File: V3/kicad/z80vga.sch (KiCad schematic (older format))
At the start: 14 parts, among them J1000 Barrel_Jack_Switch, U1000 L7805, U1001 TL760M33

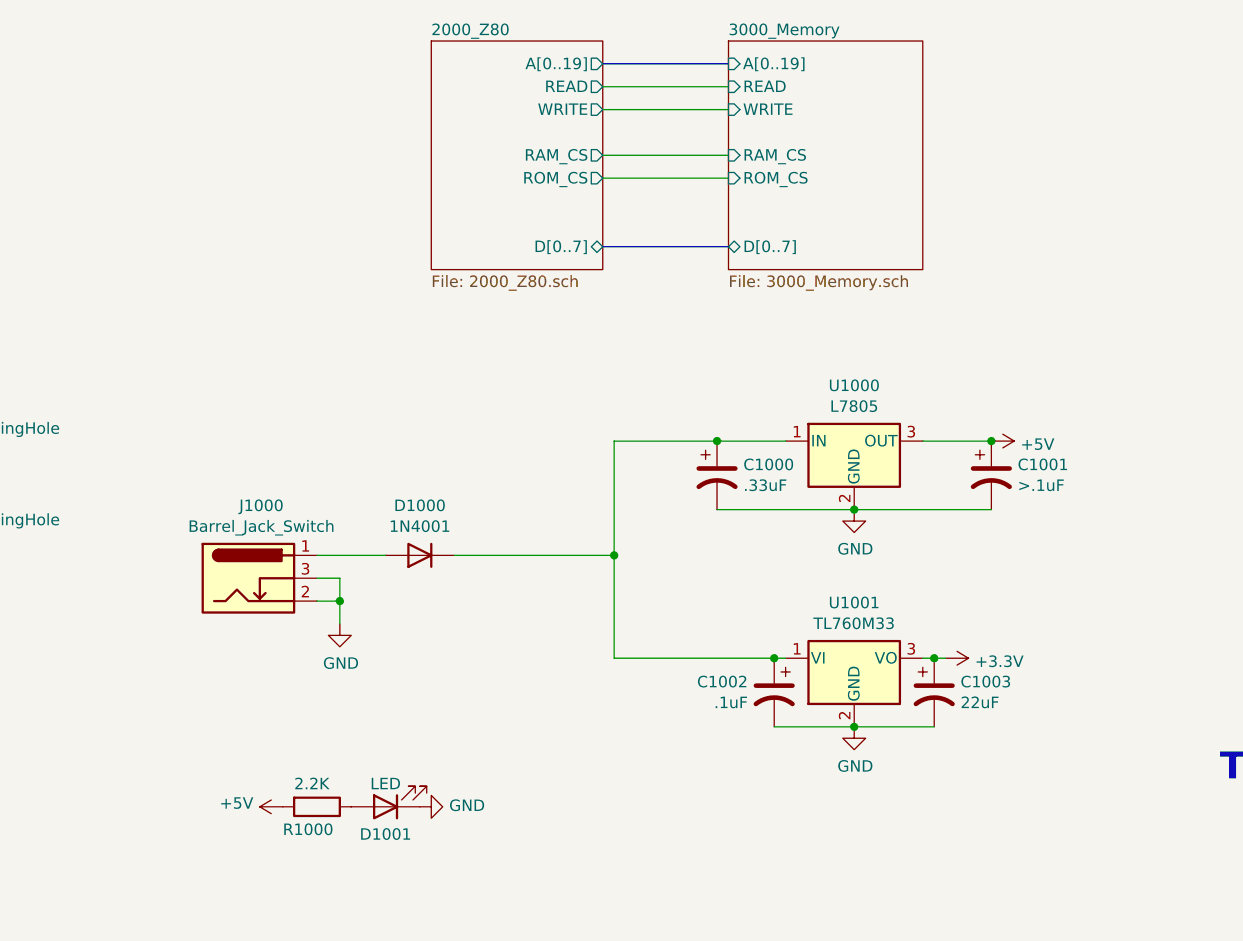
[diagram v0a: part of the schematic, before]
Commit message: 3 1 1 m memory (#15)
* moved EEPROM files to /old

* Reworking 3.0 board

* changed footprint on RAM chip

* cleared out old memory traces

* started on rerouting

* on to autoroute

* little more cleanup

* more cleanup

* ill let the autoroute do the rest

* reroute complete

* made PQFP leads fatter

* Updated GAL logic

* Design Rule Check

* Minor pcb touch up

* gerber files

* just totally redid the whole thing

* More rearranging

* added a few caps

* Routed ROM and RAM together

* more routing

* more routes

* A lot of disorganized changes

* 3.1 CSIO SPI Bus (#9)

* Updated SPI to use CPU signals

8 bit register chip controls CS lines

* Renamed and added caps to SD page

* Cleanup

* 3.1 Resistor Replacement (#10)

* First two R arrays

* Added one more r array

* added cap for SPI FF

* Extended cpu pads (#12)

* 3.1 fix sheet hierarchy (#13)

* Fixed Schematic Heirarchy issue

* some footprints re-added to board

* Add footprints added

* Minor changes

* 3.1 redraw cpu courtyard (#14)

* moved all crtyd lines to same place in file

* Duplicate lines were causing issues

* Added pin header for SPI lines

* routed last of non-bus lines

* attempted to route memory lines

* Added new symbol and footprint

* CTS0 no longer drives an LED

* Final cleanup before memory routing

* got CTS0 and RTS mixed up

* Removed extra led from board

* Updated signature

* small changes
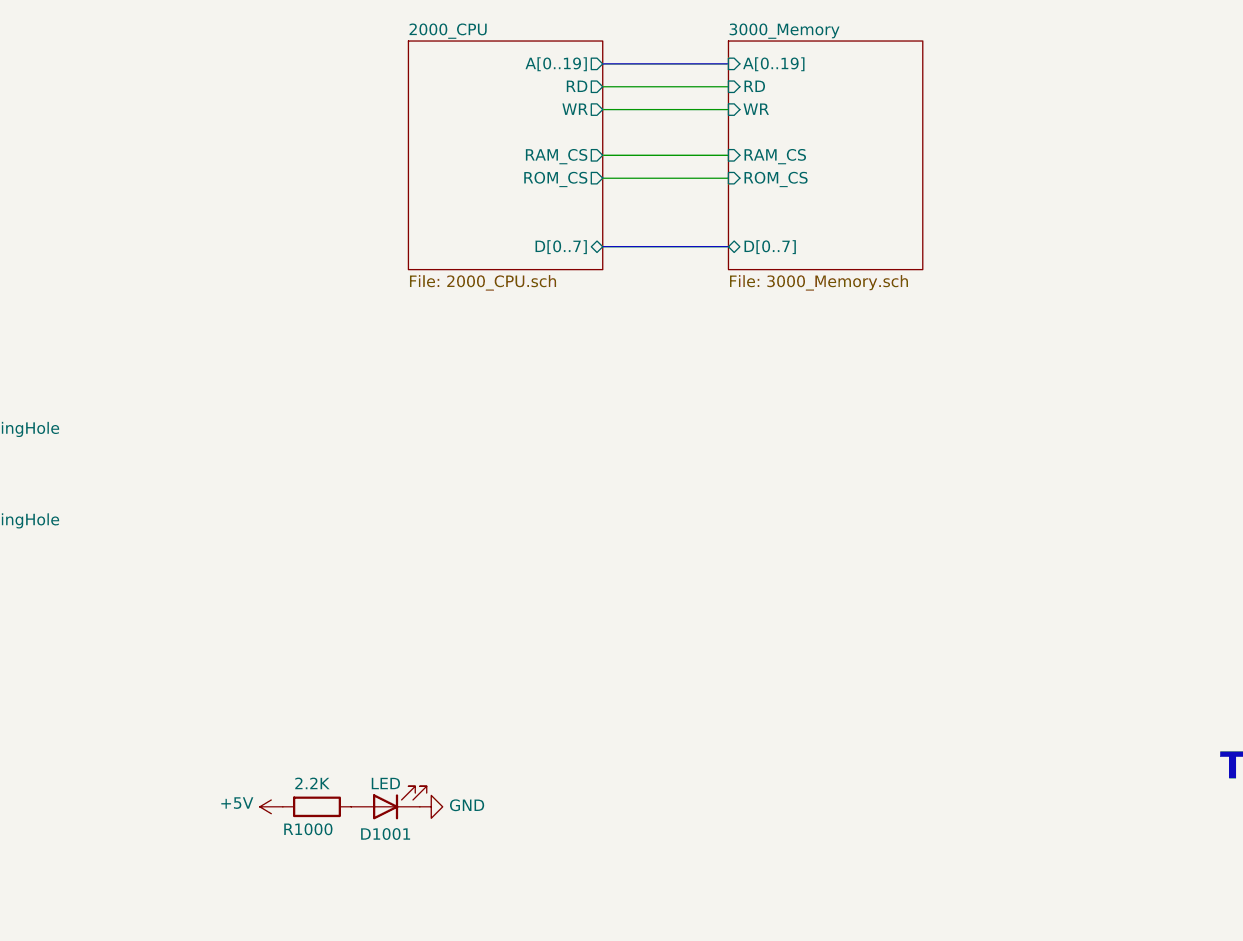
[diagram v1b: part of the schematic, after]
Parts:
- removed C1000: .33uF, Capacitor_THT:CP_Radial_D5.0mm_P2.00mm, symbol Device:CP1
- removed C1001: >.1uF, Capacitor_THT:CP_Radial_D5.0mm_P2.00mm, symbol Device:CP1
- removed C1002: .1uF, Capacitor_THT:CP_Radial_D5.0mm_P2.00mm, symbol Device:CP1
- removed C1003: 22uF, Capacitor_THT:CP_Radial_D5.0mm_P2.00mm, symbol Device:CP1
- removed D1000: 1N4001, Diode_THT:D_DO-41_SOD81_P10.16mm_Horizontal, symbol Diode:1N4001
- removed J1000: Barrel_Jack_Switch, Connector_BarrelJack:BarrelJack_Horizontal, symbol Connector:Barrel_Jack_Switch
- removed U1000: L7805, Package_TO_SOT_SMD:TO-263-3_TabPin2, symbol Regulator_Linear:L7805
- removed U1001: TL760M33, Package_TO_SOT_SMD:TO-252-3_TabPin2, symbol Regulator_Linear:LD39150DT33
- R1000: footprint Resistor_THT:R_Axial_DIN0309_L9.0mm_D3.2mm_P2.54mm_Vertical -> Resistor_SMD:R_1206_3216Metric
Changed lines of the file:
@@
 $Descr A4 11693 8268
 encoding utf-8
-Sheet 1 9
+Sheet 1 6
 Title ""
 Date ""
@@
 Wire Bus Line
 	5100 3800 5650 3800
-Wire Wire Line
-	5100 3900 5650 3900
-Wire Wire Line
-	5100 4000 5650 4000
 $Sheet
 S 5650 3700 850  1000
@@
 F3 "D[0..7]" B L 5650 4600 50
 F4 "ROM_CS" I L 5650 4300 50
-F5 "READ" I L 5650 3900 50
-F6 "RAM_CS" I L 5650 4200 50
-F7 "WRITE" I L 5650 4000 50
-$EndSheet
-$Sheet
-S 4350 3700 750  1000
-U 6191B6A2
-F0 "2000_Z80" 50
-F1 "2000_Z80.sch" 50
-F2 "D[0..7]" T R 5100 4600 50
-F3 "WRITE" O R 5100 4000 50
-F4 "READ" O R 5100 3900 50
-F5 "ROM_CS" O R 5100 4300 50
-F6 "RAM_CS" O R 5100 4200 50
-F7 "A[0..19]" O R 5100 3800 50
+F5 "RAM_CS" I L 5650 4200 50
+F6 "RD" I L 5650 3900 50
+F7 "WR" I L 5650 4000 50
 $EndSheet
 Text Notes 7800 6950 0    118  ~ 24
@@
 Wire Wire Line
 	5100 4300 5650 4300
-$Comp
-L Regulator_Linear:L7805 U1000
-U 1 1 6255C02F
-P 6200 5450
-F 0 "U1000" H 6200 5692 50  0000 C CNN
-F 1 "L7805" H 6200 5601 50  0000 C CNN
-F 2 "Package_TO_SOT_SMD:TO-263-3_TabPin2" H 6225 5300 50  0001 L CIN
-F 3 "http://www.st.com/content/ccc/resource/technical/document/datasheet/41/4f/b3/b0/12/d4/47/88/CD00000444.pdf/files/CD00000444.pdf/jcr:content/translations/en.CD00000444.pdf" H 6200 5400 50  0001 C CNN
-	1    6200 5450
-	1    0    0    -1
-$EndComp
-$Comp
-L Device:CP1 C1000
-U 1 1 6255CCA4
-P 5600 5600
-F 0 "C1000" H 5715 5646 50  0000 L CNN
-F 1 ".33uF" H 5715 5555 50  0000 L CNN
-F 2 "Capacitor_THT:CP_Radial_D5.0mm_P2.00mm" H 5600 5600 50  0001 C CNN
-F 3 "~" H 5600 5600 50  0001 C CNN
-	1    5600 5600
-	1    0    0    -1
-$EndComp
-$Comp
-L Device:CP1 C1001
-U 1 1 6255DB35
-P 6800 5600
-F 0 "C1001" H 6915 5646 50  0000 L CNN
-F 1 ">.1uF" H 6915 5555 50  0000 L CNN
-F 2 "Capacitor_THT:CP_Radial_D5.0mm_P2.00mm" H 6800 5600 50  0001 C CNN
-F 3 "~" H 6800 5600 50  0001 C CNN
-	1    6800 5600
-	1    0    0    -1
-$EndComp
-Wire Wire Line
-	5600 5450 5900 5450
-Wire Wire Line
-	6500 5450 6800 5450
-Wire Wire Line
-	5600 5750 6200 5750
-Connection ~ 6200 5750
-Wire Wire Line
-	6200 5750 6800 5750
-$Comp
-L power:GND #PWR0119
-U 1 1 6255E2E4
-P 6200 5750
-F 0 "#PWR0119" H 6200 5500 50  0001 C CNN
-F 1 "GND" H 6205 5577 50  0000 C CNN
-F 2 "" H 6200 5750 50  0001 C CNN
-F 3 "" H 6200 5750 50  0001 C CNN
-	1    6200 5750
-	1    0    0    -1
-$EndComp
-$Comp
-L power:+5V #PWR0141
-U 1 1 6255EB09
-P 6800 5450
-F 0 "#PWR0141" H 6800 5300 50  0001 C CNN
-F 1 "+5V" V 6815 5578 50  0000 L CNN
-F 2 "" H 6800 5450 50  0001 C CNN
-F 3 "" H 6800 5450 50  0001 C CNN
-	1    6800 5450
-	0    1    1    0
-$EndComp
-Connection ~ 6800 5450
-$Comp
-L Connector:Barrel_Jack_Switch J1000
-U 1 1 62560114
-P 3550 6050
-F 0 "J1000" H 3607 6367 50  0000 C CNN
-F 1 "Barrel_Jack_Switch" H 3607 6276 50  0000 C CNN
-F 2 "Connector_BarrelJack:BarrelJack_Horizontal" H 3600 6010 50  0001 C CNN
-F 3 "~" H 3600 6010 50  0001 C CNN
-	1    3550 6050
-	1    0    0    -1
-$EndComp
-Wire Wire Line
-	3850 5950 4150 5950
-Wire Wire Line
-	3850 6050 3950 6050
-Wire Wire Line
-	3950 6050 3950 6150
-Wire Wire Line
-	3950 6150 3850 6150
-Wire Wire Line
-	3950 6150 3950 6250
-Connection ~ 3950 6150
-$Comp
-L Diode:1N4001 D1000
-U 1 1 62563A78
-P 4300 5950
-F 0 "D1000" H 4300 5733 50  0000 C CNN
-F 1 "1N4001" H 4300 5824 50  0000 C CNN
-F 2 "Diode_THT:D_DO-41_SOD81_P10.16mm_Horizontal" H 4300 5775 50  0001 C CNN
-F 3 "http://www.vishay.com/docs/88503/1n4001.pdf" H 4300 5950 50  0001 C CNN
-	1    4300 5950
-	-1   0    0    1
-$EndComp
 $Comp
 L Mechanical:MountingHole H0
@@
 F 0 "R1000" V 3950 6900 50  0000 L CNN
 F 1 "2.2K" V 3750 6950 50  0000 L CNN
-F 2 "Resistor_THT:R_Axial_DIN0309_L9.0mm_D3.2mm_P2.54mm_Vertical" V 3780 7050 50  0001 C CNN
+F 2 "Resistor_SMD:R_1206_3216Metric" V 3780 7050 50  0001 C CNN
 F 3 "~" H 3850 7050 50  0001 C CNN
 	1    3850 7050
 	0    1    1    0
 $EndComp
-$Comp
-L Regulator_Linear:LD39150DT33 U?
-U 1 1 6290B173
-P 6200 6400
-AR Path="/6191B6A2/61F28B7D/6290B173" Ref="U?"  Part="1"
-AR Path="/6191B6A2/61F28B7D/62590ED9/6290B173" Ref="U?"  Part="1"
-AR Path="/6290B173" Ref="U1001"  Part="1"
-F 0 "U1001" H 6200 6642 50  0000 C CNN
-F 1 "TL760M33" H 6200 6551 50  0000 C CNN
-F 2 "Package_TO_SOT_SMD:TO-252-3_TabPin2" H 6200 6600 50  0001 C CNN
-F 3 "https://www.st.com/resource/en/datasheet/ld39150.pdf" H 6300 6150 50  0001 C CNN
-	1    6200 6400
-	1    0    0    -1
-$EndComp
-$Comp
-L power:+3.3V #PWR?
-U 1 1 6290B179
-P 6600 6400
-AR Path="/6191B6A2/61F28B7D/6290B179" Ref="#PWR?"  Part="1"
-AR Path="/6191B6A2/61F28B7D/62590ED9/6290B179" Ref="#PWR?"  Part="1"
-AR Path="/6290B179" Ref="#PWR0120"  Part="1"
-F 0 "#PWR0120" H 6600 6250 50  0001 C CNN
-F 1 "+3.3V" V 6615 6528 50  0000 L CNN
-F 2 "" H 6600 6400 50  0001 C CNN
-F 3 "" H 6600 6400 50  0001 C CNN
-	1    6600 6400
-	0    1    1    0
-$EndComp
-$Comp
-L power:GND #PWR?
-U 1 1 6290B17F
-P 6200 6700
-AR Path="/6191B6A2/61F28B7D/6290B17F" Ref="#PWR?"  Part="1"
-AR Path="/6191B6A2/61F28B7D/62590ED9/6290B17F" Ref="#PWR?"  Part="1"
-AR Path="/6290B17F" Ref="#PWR0124"  Part="1"
-F 0 "#PWR0124" H 6200 6450 50  0001 C CNN
-F 1 "GND" H 6205 6527 50  0000 C CNN
-F 2 "" H 6200 6700 50  0001 C CNN
-F 3 "" H 6200 6700 50  0001 C CNN
-	1    6200 6700
-	1    0    0    -1
-$EndComp
 Wire Wire Line
-	5850 6700 6200 6700
+	5100 3900 5650 3900
 Wire Wire Line
-	6200 6700 6550 6700
-Connection ~ 6200 6700
-$Comp
-L Device:CP1 C1003
-U 1 1 6290B18E
-P 6550 6550
-AR Path="/6290B18E" Ref="C1003"  Part="1"
-AR Path="/6191B6A2/61F28B7D/62590ED9/6290B18E" Ref="C?"  Part="1"
-F 0 "C1003" H 6665 6596 50  0000 L CNN
-F 1 "22uF" H 6665 6505 50  0000 L CNN
-F 2 "Capacitor_THT:CP_Radial_D5.0mm_P2.00mm" H 6550 6550 50  0001 C CNN
-F 3 "~" H 6550 6550 50  0001 C CNN
-	1    6550 6550
-	1    0    0    -1
-$EndComp
-Wire Wire Line
-	6500 6400 6550 6400
-Connection ~ 6550 6400
-Wire Wire Line
-	6550 6400 6600 6400
-Wire Wire Line
-	5850 6400 5900 6400
-$Comp
-L Device:CP1 C1002
-U 1 1 6290B196
-P 5850 6550
-AR Path="/6290B196" Ref="C1002"  Part="1"
-AR Path="/6191B6A2/61F28B7D/62590ED9/6290B196" Ref="C?"  Part="1"
-F 0 "C1002" H 5965 6596 50  0000 L CNN
-F 1 ".1uF" H 5965 6505 50  0000 L CNN
-F 2 "Capacitor_THT:CP_Radial_D5.0mm_P2.00mm" H 5850 6550 50  0001 C CNN
-F 3 "~" H 5850 6550 50  0001 C CNN
-	1    5850 6550
-	-1   0    0    -1
-$EndComp
-$Comp
-L power:GND #PWR0140
-U 1 1 629120EB
-P 3950 6250
-F 0 "#PWR0140" H 3950 6000 50  0001 C CNN
-F 1 "GND" H 3955 6077 50  0000 C CNN
-F 2 "" H 3950 6250 50  0001 C CNN
-F 3 "" H 3950 6250 50  0001 C CNN
-	1    3950 6250
-	1    0    0    -1
-$EndComp
-Wire Wire Line
-	4450 5950 5150 5950
-Wire Wire Line
-	5150 5950 5150 5450
-Wire Wire Line
-	5150 5450 5600 5450
-Connection ~ 5600 5450
-Wire Wire Line
-	5150 5950 5150 6400
-Wire Wire Line
-	5150 6400 5850 6400
-Connection ~ 5150 5950
-Connection ~ 5850 6400
+	5100 4000 5650 4000
+$Sheet
+S 4250 3700 850  1000
+U 63A83936
+F0 "2000_CPU" 50
+F1 "2000_CPU.sch" 50
+F2 "A[0..19]" O R 5100 3800 50
+F3 "RD" O R 5100 3900 50
+F4 "ROM_CS" O R 5100 4300 50
+F5 "RAM_CS" O R 5100 4200 50
+F6 "D[0..7]" B R 5100 4600 50
+F7 "WR" O R 5100 4000 50
+$EndSheet
 $EndSCHEMATC
